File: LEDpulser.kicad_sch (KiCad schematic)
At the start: 69 parts, among them J1 RJHSE5380, J2 EPS.00.250.NTN, J3 EPS.00.250.NTN, J4 Conn_01x04_Female, J5 LED, Q1 AO3401A, Q2 AO3400A, Q3 AO3400A, SW1 BST11T2AVR, U1 SN74AHCT123A, U10 LT3082, U2 SN74AHCT123A, U3 SN74AHCT123A, U4 SN74HCS72, U5 LT1121-5, U6 PM8834, U7 NE555, U8 PM8834, U9 PM8834

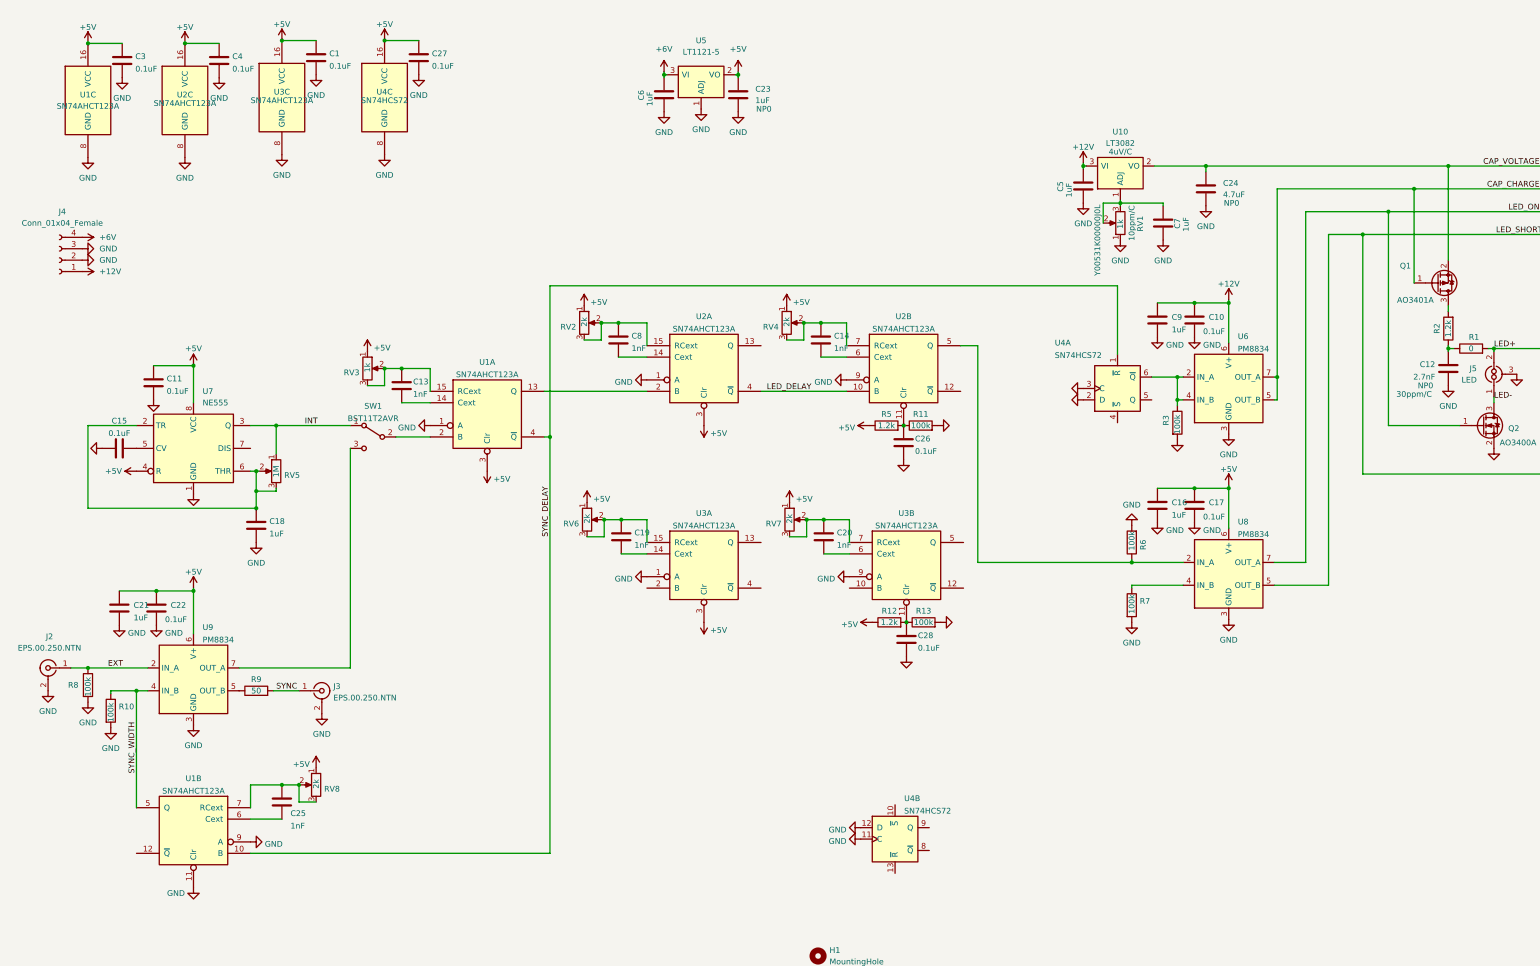
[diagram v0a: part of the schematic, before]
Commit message: Updated Schematic, started placement.
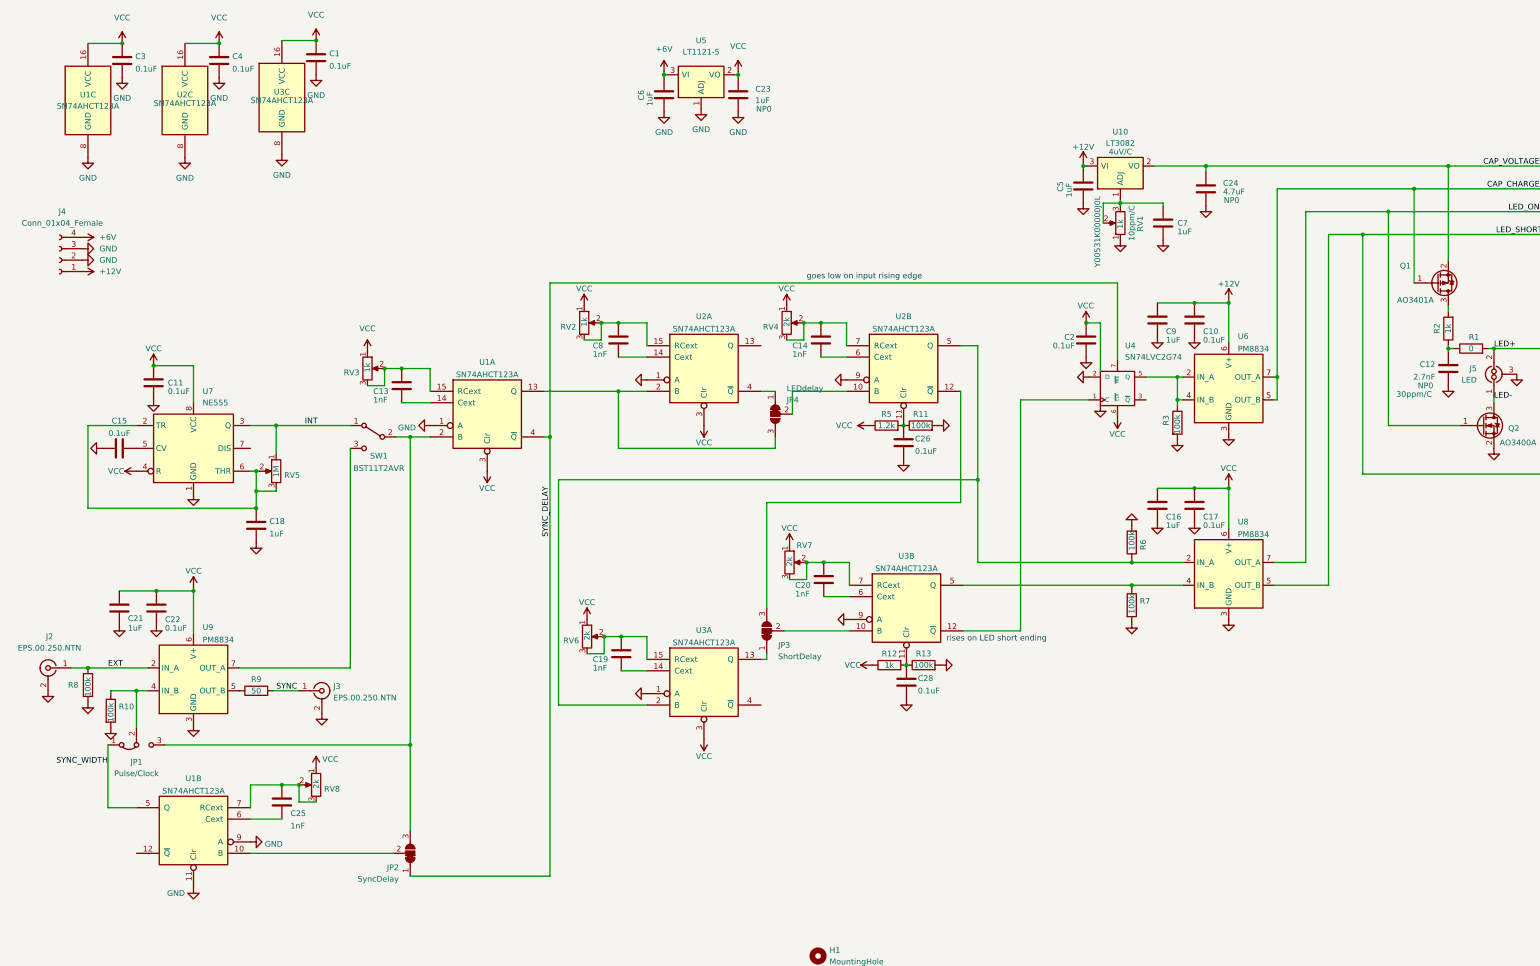
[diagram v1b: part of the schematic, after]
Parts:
- removed C27: 0.1uF, Capacitor_SMD:C_0603_1608Metric, symbol Device:C
- removed U4: SN74HCS72, Package_SO:TSSOP-16-1EP_4.4x5mm_P0.65mm, symbol 74xx:74HC74
- added C2: 0.1uF, Capacitor_SMD:C_0603_1608Metric, symbol Device:C
- added JP1: Pulse/Clock, Connector_PinHeader_2.54mm:PinHeader_1x03_P2.54mm_Vertical, symbol Jumper:Jumper_3_Bridged12
- added JP2: SyncDelay, Jumper:SolderJumper-3_P1.3mm_Bridged12_RoundedPad1.0x1.5mm, symbol Jumper:SolderJumper_3_Bridged12
- added JP3: ShortDelay, Jumper:SolderJumper-3_P1.3mm_Bridged12_RoundedPad1.0x1.5mm, symbol Jumper:SolderJumper_3_Bridged12
- added JP4: LEDdelay, Jumper:SolderJumper-3_P1.3mm_Bridged12_RoundedPad1.0x1.5mm, symbol Jumper:SolderJumper_3_Bridged12
- added U4: SN74LVC2G74, Package_SO:SSOP-8_2.95x2.8mm_P0.65mm, symbol 74xGxx:74LVC2G74
- R11, R13, R5: footprint (none) -> Resistor_SMD:R_0603_1608Metric
- R12: value 1.2k -> 1k; footprint (none) -> Resistor_SMD:R_0603_1608Metric
- R2: value 1.2k -> 1k
- RV2: value 2k -> 1k; footprint Potentiometer_THT:Potentiometer_Bourns_3266X_Horizontal -> Potentiometer_THT:Potentiometer_Bourns_3266W_Vertical
- RV4, RV6, RV7: footprint Potentiometer_THT:Potentiometer_Bourns_3266X_Horizontal -> Potentiometer_THT:Potentiometer_Bourns_3266W_Vertical
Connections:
- net GND: now also C2.2, U4.2 (D), U4.4 (GND)
- net SYNC_DELAY: now also JP2.1 (A), U4.7 (~{PRE}); no longer U1.10 (B)
- net SYNC_WIDTH: now also JP1.1 (A); no longer R10.1, U9.4 (IN_B)
- net at U2.12 (~{Q}): now also JP3.3 (B)
- net at R6.1, U2.5 (Q), U8.2 (IN_A): now also U3.2 (B)
- net at U1.13 (Q), U2.2 (B): now also JP4.3 (B)
- net at R7.1, U8.4 (IN_B): now also U3.5 (Q)
- net at U3.13 (Q): now also JP3.1 (A)
- net at R3.1, U6.2 (IN_A), U6.4 (IN_B): now also U4.5 (Q)
- net at SW1.2 (B), U1.2 (B): now also JP1.3 (B), JP2.3 (B)
- net at U3.10 (B): now also JP3.2 (C)
- net at U3.12 (~{Q}): now also U4.1 (C)
- net +5V renamed VCC
- net VCC: now also C2.1, U4.6 (~{CLR}), U4.8 (VCC)
- net LED_DELAY: no longer names the net of U2.10 (B)
- net LED_DELAY: now also JP4.2 (C); no longer U2.4 (~{Q})
- new net: JP4.1 (A), U2.4 (~{Q})
- new net: JP2.2 (C), U1.10 (B)
- new net: JP1.2 (C), R10.1, U9.4 (IN_B)
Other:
- note added: "goes low on input rising edge"
- note added: "rises on LED short ending"
- moved on the sheet: C19, C20, C28, R12, R13, RV6, RV7, U3A, U3B

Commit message: Modified logic to use flip-flop and reduce front panel adjustments. Changed to +24V for LED capacitor charge supply. Selected components. Rough layout.
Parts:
- removed C28: 0.1uF, Capacitor_SMD:C_0603_1608Metric, symbol Device:C
- removed JP1: Pulse/Clock, Connector_PinHeader_2.54mm:PinHeader_1x03_P2.54mm_Vertical, symbol Jumper:Jumper_3_Bridged12
- removed JP2: SyncDelay, Jumper:SolderJumper-3_P1.3mm_Bridged12_RoundedPad1.0x1.5mm, symbol Jumper:SolderJumper_3_Bridged12
- removed JP3: ShortDelay, Jumper:SolderJumper-3_P1.3mm_Bridged12_RoundedPad1.0x1.5mm, symbol Jumper:SolderJumper_3_Bridged12
- removed JP4: LEDdelay, Jumper:SolderJumper-3_P1.3mm_Bridged12_RoundedPad1.0x1.5mm, symbol Jumper:SolderJumper_3_Bridged12
- removed R11, R13: 100k, Resistor_SMD:R_0603_1608Metric, symbol Device:R
- removed R12: 1k, Resistor_SMD:R_0603_1608Metric, symbol Device:R
- added D1, D2: CUS08F30,H3F, Diode_SMD:D_SOD-323, symbol Diode:BAT48JFILM
- C18: value 1uF -> 22uF; footprint Capacitor_SMD:C_0603_1608Metric -> Capacitor_SMD:C_0805_2012Metric; Dielectric (none) -> X5R
- C24: value 4.7uF -> 22uF; footprint Capacitor_SMD:C_0603_1608Metric -> Capacitor_SMD:C_0805_2012Metric; Dielectric NP0 -> X5R
- J1: value RJHSE5380 -> RJHSE-5380; Name (none) -> Timing/Amplitude Output
- J2: Name (none) -> External Trigger Input
- J3: Name (none) -> Sync Pulse Output
- J4: value Conn_01x04_Female -> EB21A-04-D
- J5: value LED -> EPL.0S.302.HLN; Name (none) -> Out to LED; Part# EPL.0S.302.HLN -> (none)
- Q1: value AO3401A -> BVSS84LT1G; VGS(th) (none) -> VGS(th) -0.9V to -2.0V
- Q2, Q3: value AO3400A -> DMN3028LQ-7
- R5: value 1.2k -> 100k
- R9: footprint Resistor_SMD:R_0603_1608Metric -> Resistor_SMD:R_1206_3216Metric
- RV1: value 1k -> 2k; Part# Y00531K00000J0L -> Y50532K00000J0L
- RV2, RV3: value 1k -> 500; Part# 64XR2KLF -> 3262X-1-501LF
- RV4, RV6, RV7: Part# 64XR2KLF -> 3296Y-1-202LF
- RV5: value 1M -> 50k; Part# 3262X-1-105LF -> 3262X-1-503LF
- RV8: Part# 64XR2KLF -> 3262X-1-202LF
- SW1: PartNumber BST11T2AVR -> (none)
- U1, U2, U3: value SN74AHCT123A -> 74AHCT123APW,118
- U10: value LT3082 -> LT3082EST#TRPBF
- U5: value LT1121-5 -> LT1121CST-5#TRPBF
- U6: value PM8834 -> IXDI602SIATR
- U7: value NE555 -> NE555S-13; footprint Package_SO:SOIC-8_3.9x4.9mm_P1.27mm -> Package_SO:SO-8_3.9x4.9mm_P1.27mm
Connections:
- net SYNC_WIDTH is gone; now on net SYNC: U1.5 (Q)
- net GND: now also R5.2
- net LED_ON: now also R6.1, U2.5 (Q), U8.2 (IN_A); no longer J1.4, Q2.1 (G), U8.7 (OUT_A)
- net LED_SHORT: now also R7.1, U3.5 (Q), U8.4 (IN_B); no longer J1.2, Q3.1 (G), U8.5 (OUT_B)
- net SYNC: now also R10.1, U9.4 (IN_B); no longer J3.1 (In), R9.2
- net SYNC_DELAY: now also U1.10 (B)
- net VCC: now also U2.11 (Clr), U3.11 (Clr), D1.2 (A); no longer R5.1
- net at U2.10 (B): now also U2.4 (~{Q}), U3.2 (B)
- net at U2.14 (Cext): now also C8.1; no longer C8.2
- net at RV2.2, RV2.3, U2.15 (RCext): now also C8.2; no longer C8.1
- net CAP_CHARGE_ON: now reaches U3.12 (~{Q}), U4.1 (C)
- net at R3.1, U4.5 (Q), U6.2 (IN_A): no longer U6.4 (IN_B)
- net LED_SHORT_DELAY: now reaches U3.13 (Q)
- net LED_SHORT_DELAY: now also U3.10 (B)
- net INPUT: now reaches SW1.2 (B), U1.2 (B)
- net EXTERNAL: now reaches SW1.3 (C), U9.7 (OUT_A)
- net +12V: no longer names the net of C10.1, C9.1, U6.6 (V+)
- net +12V: now also D1.1 (K), D2.1 (K); no longer C5.1, J4.1 (Pin_1), U10.3 (VI)
- net CAP_CHARGE renamed CAP_CHARGING_OUT
- net CAP_CHARGING_OUT: no longer U6.5 (OUT_B)
- net CAP_VOLTAGE renamed CAP_VOLTAGE_OUT
- net CAP_VOLTAGE_OUT: now also C26.1, D2.2 (A)
- net EXT: no longer names the net of J2.1 (In), R8.1, U9.2 (IN_A)
- net INT renamed INTERNAL
- new net: R5.1, U6.4 (IN_B)
- new net: J3.1 (In), R9.2
- new net +24V: C5.1, J4.1 (Pin_1), U10.3 (VI)
- new net LED_ON_OUT: J1.4, Q2.1 (G), U8.7 (OUT_A)
- new net LED_SHORT_OUT: J1.2, Q3.1 (G), U8.5 (OUT_B)
- no-connect marks 0 -> 7
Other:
- note added: "rises on end of LED short"
- note removed: "rises on LED short ending"
- moved on the sheet: C1, C11, C12, C13, C14, C15, C16, C18, C19, C2, C20, C24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

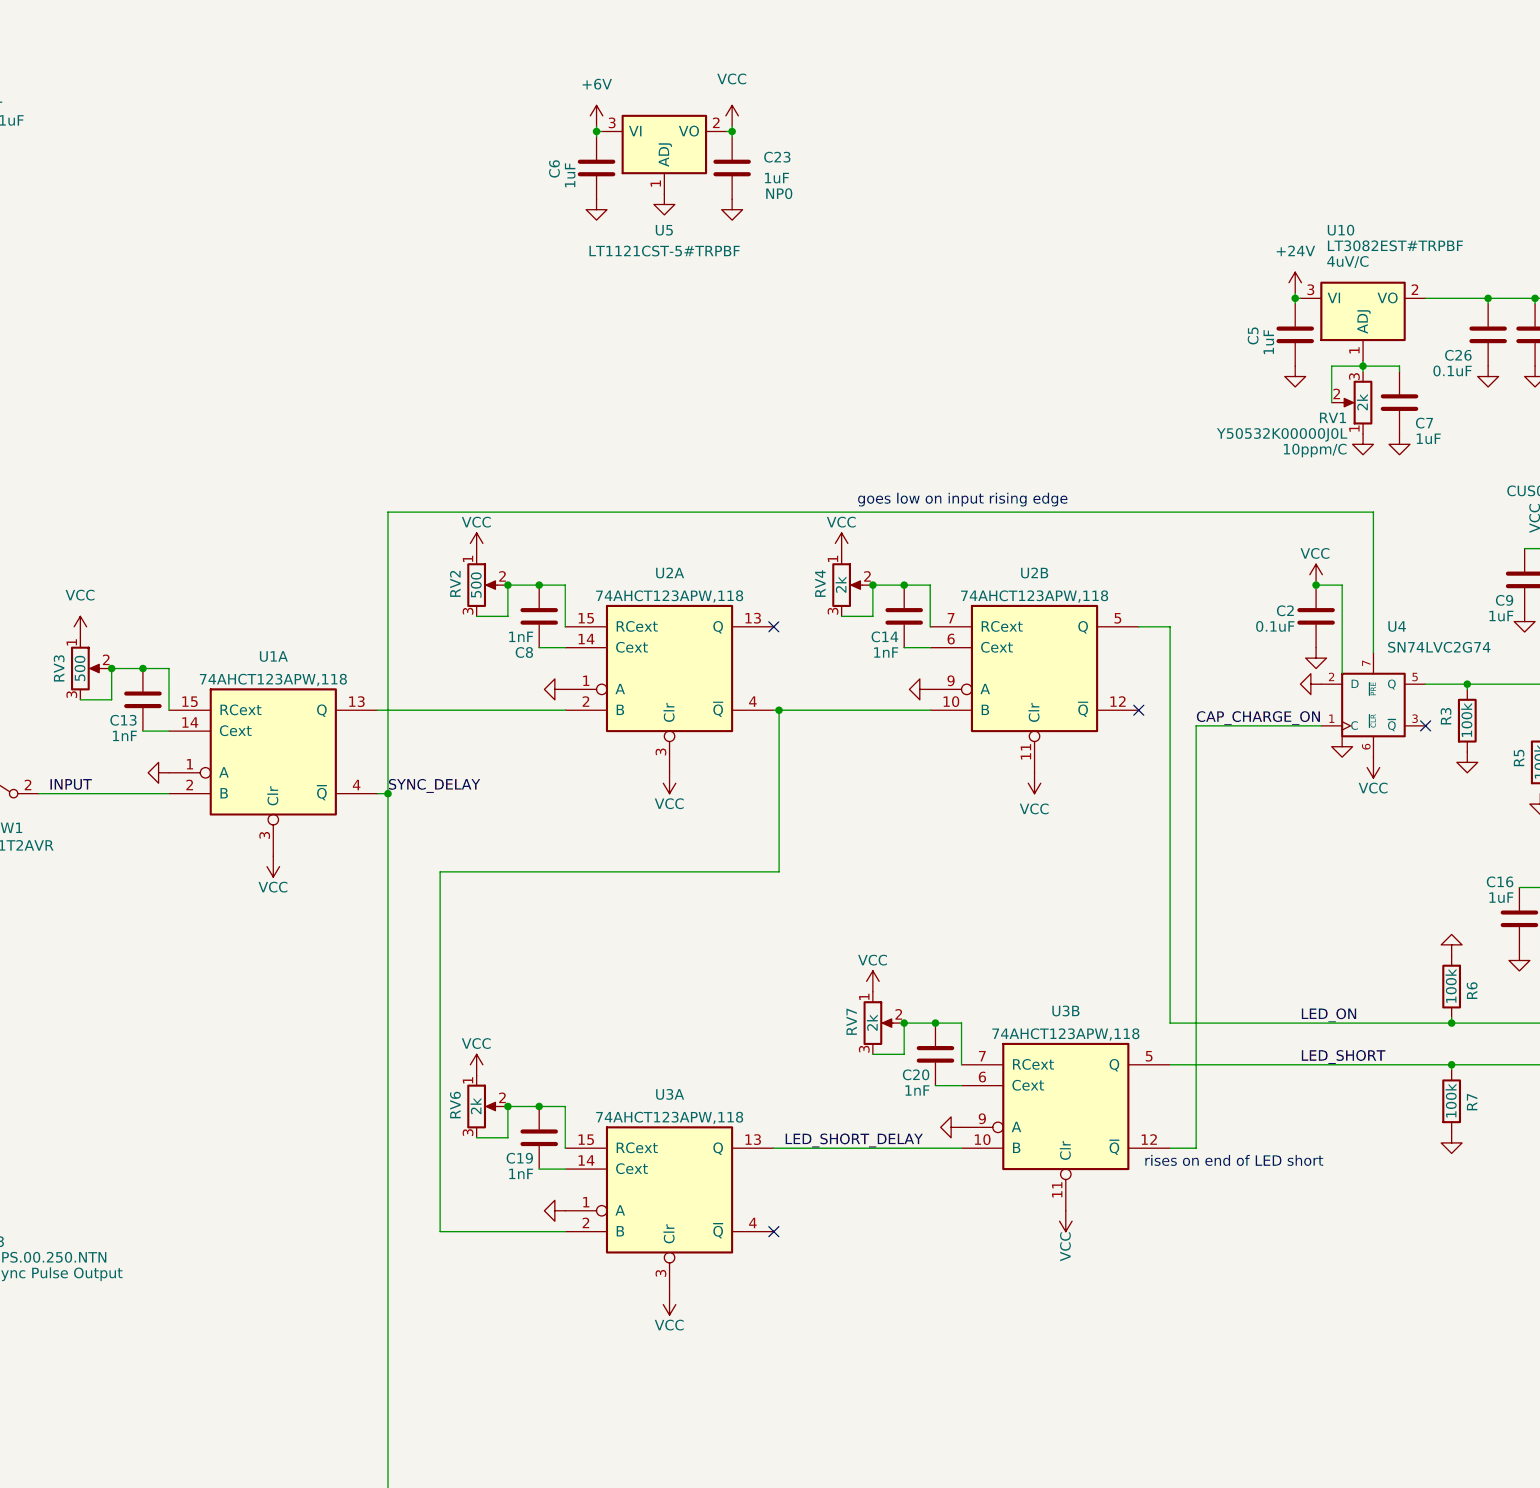
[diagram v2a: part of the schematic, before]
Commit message: Fixed logic on LED short delay and added startup inhibit to set initial states.
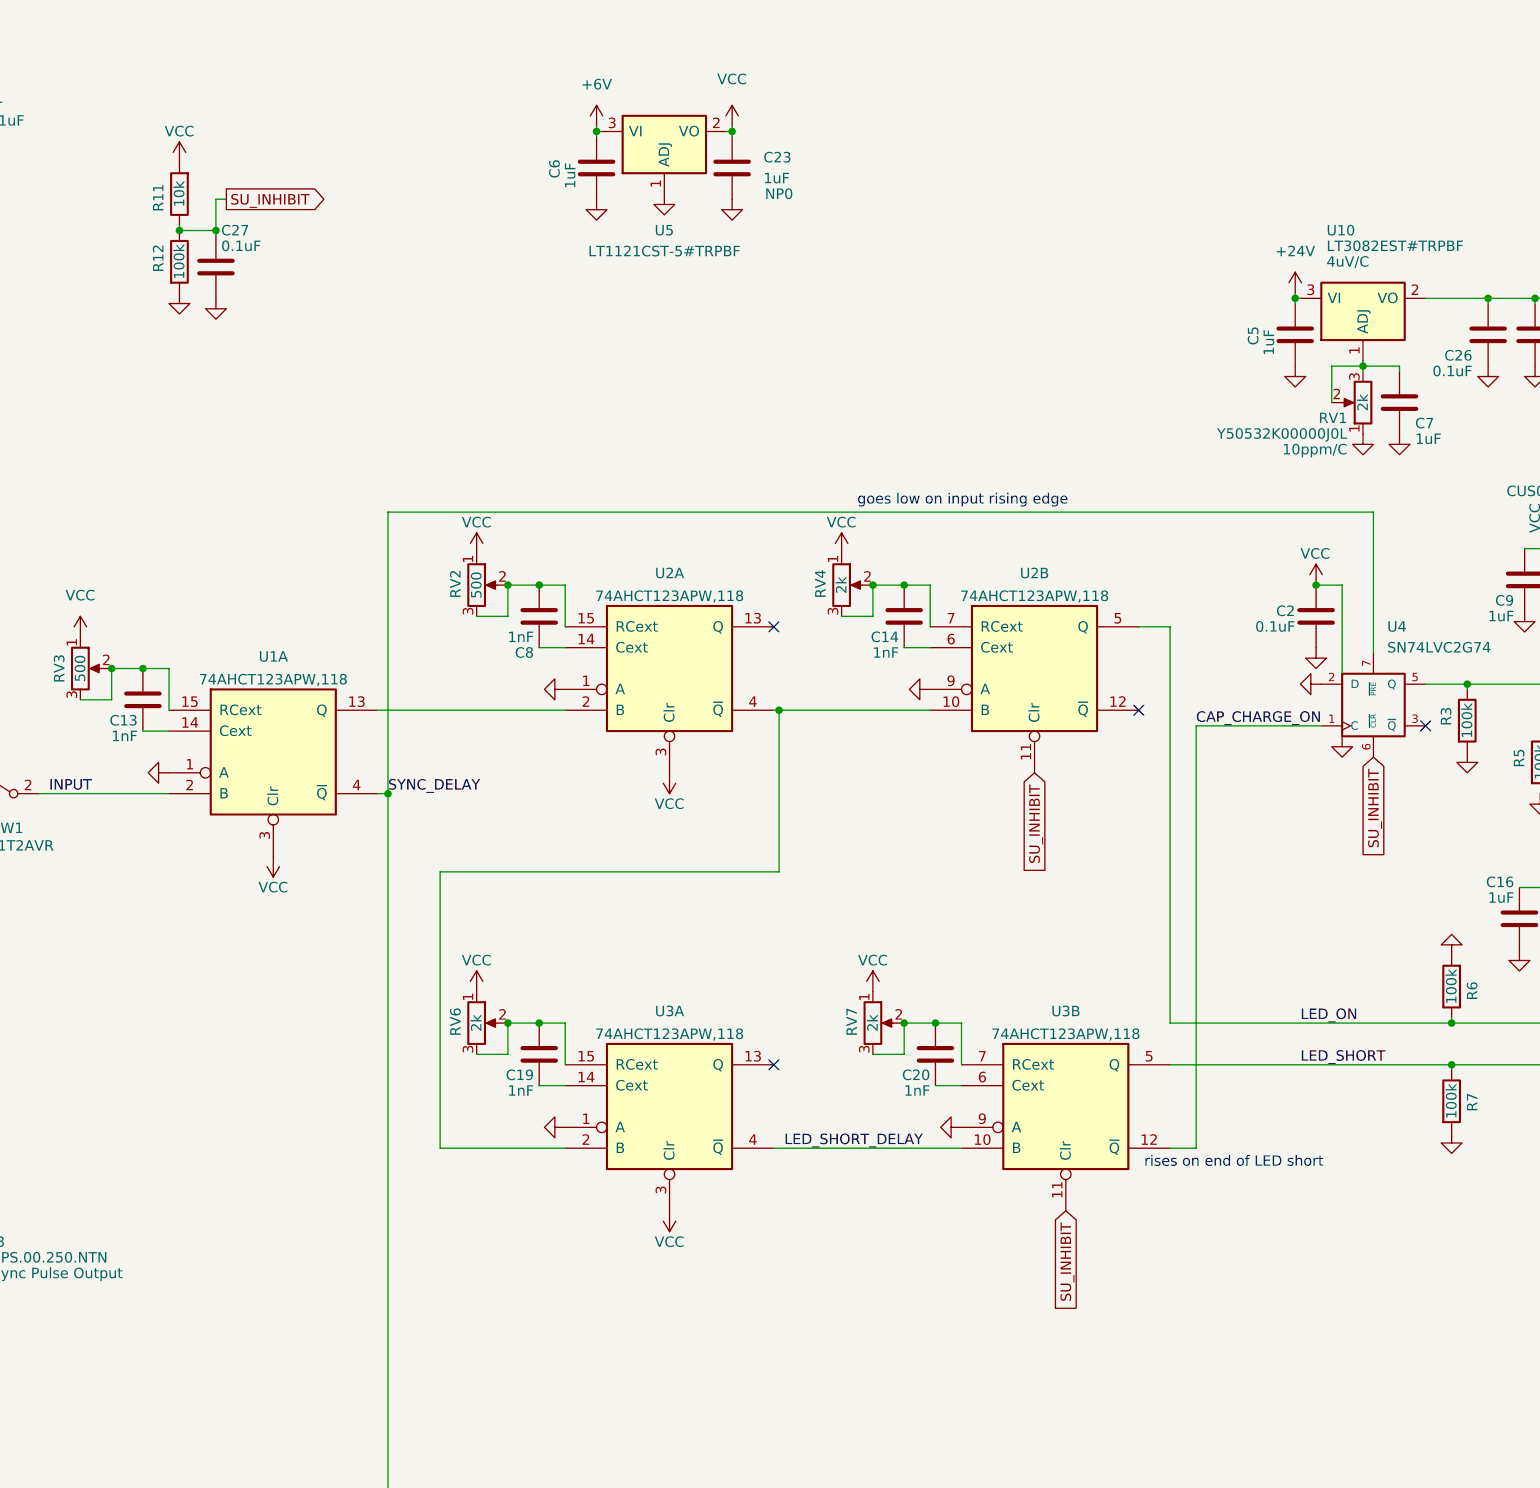
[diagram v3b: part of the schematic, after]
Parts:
- added C27: 0.1uF, Capacitor_SMD:C_0603_1608Metric, symbol Device:C
- added R11: 10k, Resistor_SMD:R_0603_1608Metric, symbol Device:R
- added R12: 100k, Resistor_SMD:R_0603_1608Metric, symbol Device:R
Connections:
- net GND: now also C27.2, R12.2
- net LED_SHORT_DELAY: now also U3.4 (~{Q}); no longer U3.13 (Q)
- net VCC: now also R11.2; no longer U2.11 (Clr), U3.11 (Clr), U4.6 (~{CLR})
- new net SU_INHIBIT: C27.1, R11.1, R12.1, U2.11 (Clr), U3.11 (Clr), U4.6 (~{CLR})
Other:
- moved on the sheet: C19, RV6, U3A
